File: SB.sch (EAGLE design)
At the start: 59 parts, among them IC1 ATMEGA32U4NT-TQFP, IC2 MCP2515, IC3 MCP2551, J1 USB-B-PTH, X1 INPUT, X2 OUTPUT

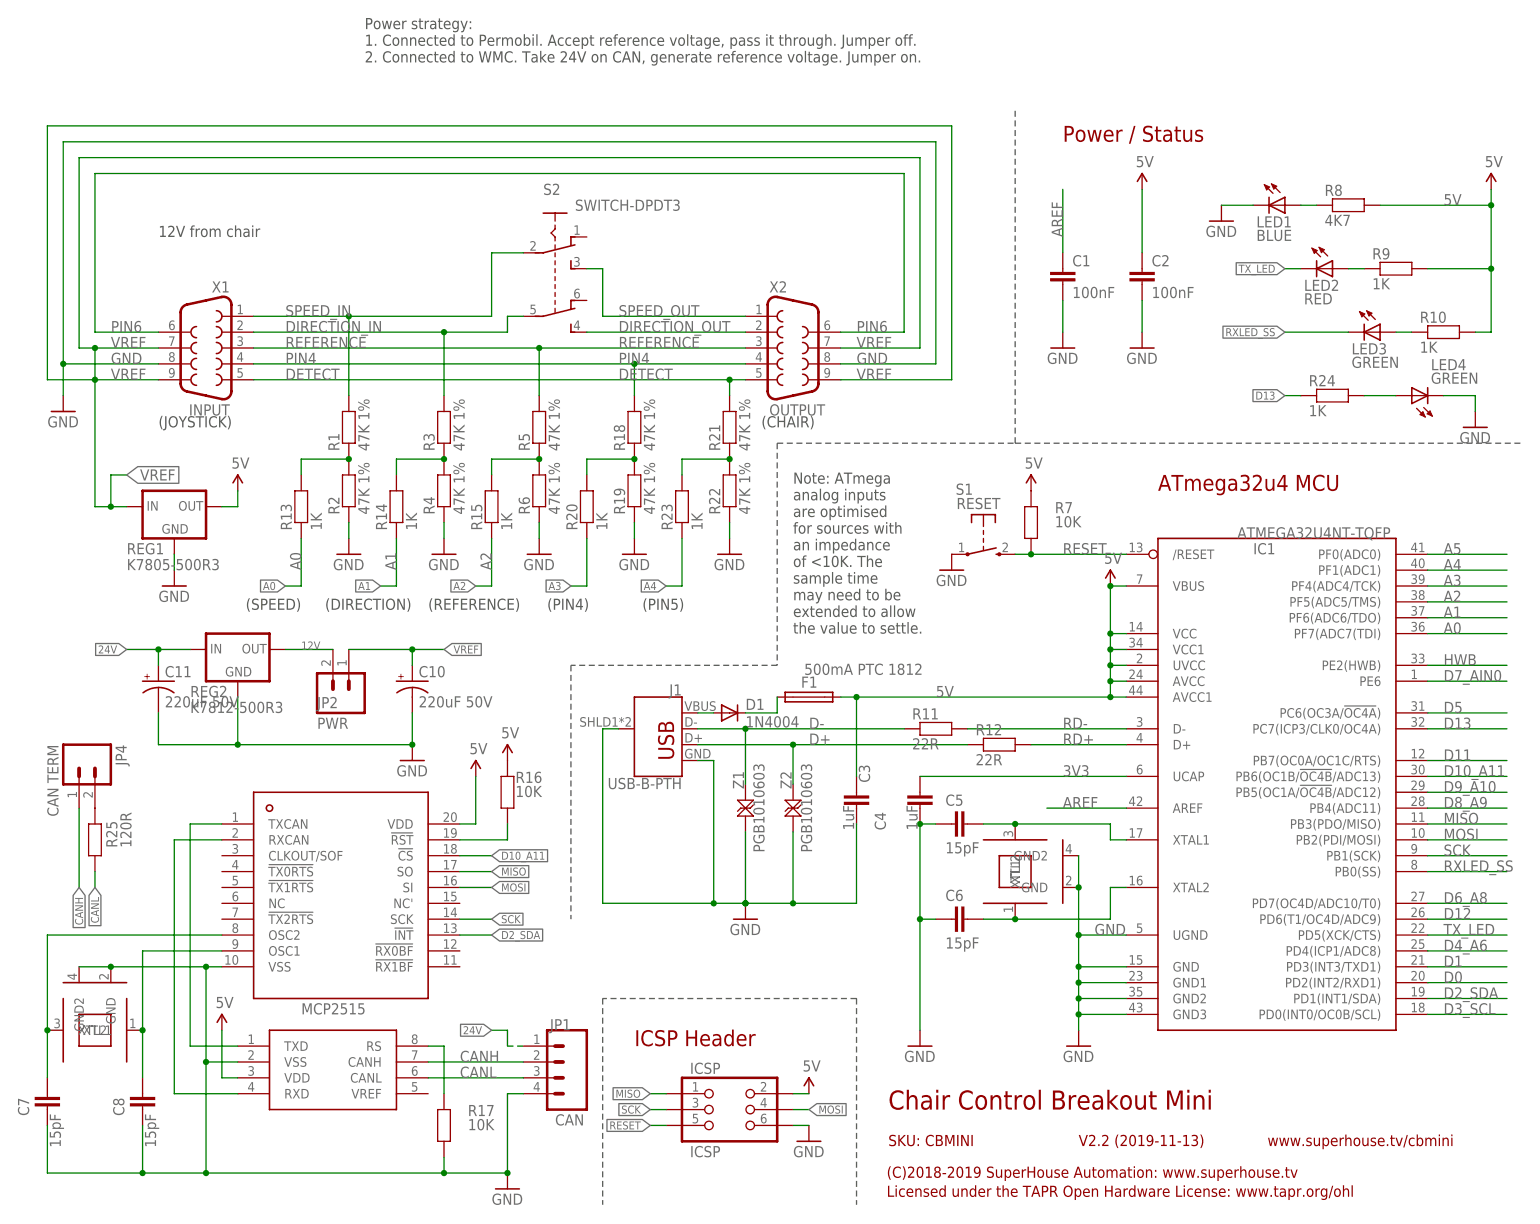
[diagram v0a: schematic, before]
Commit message: Basic schematic done and rough board outline
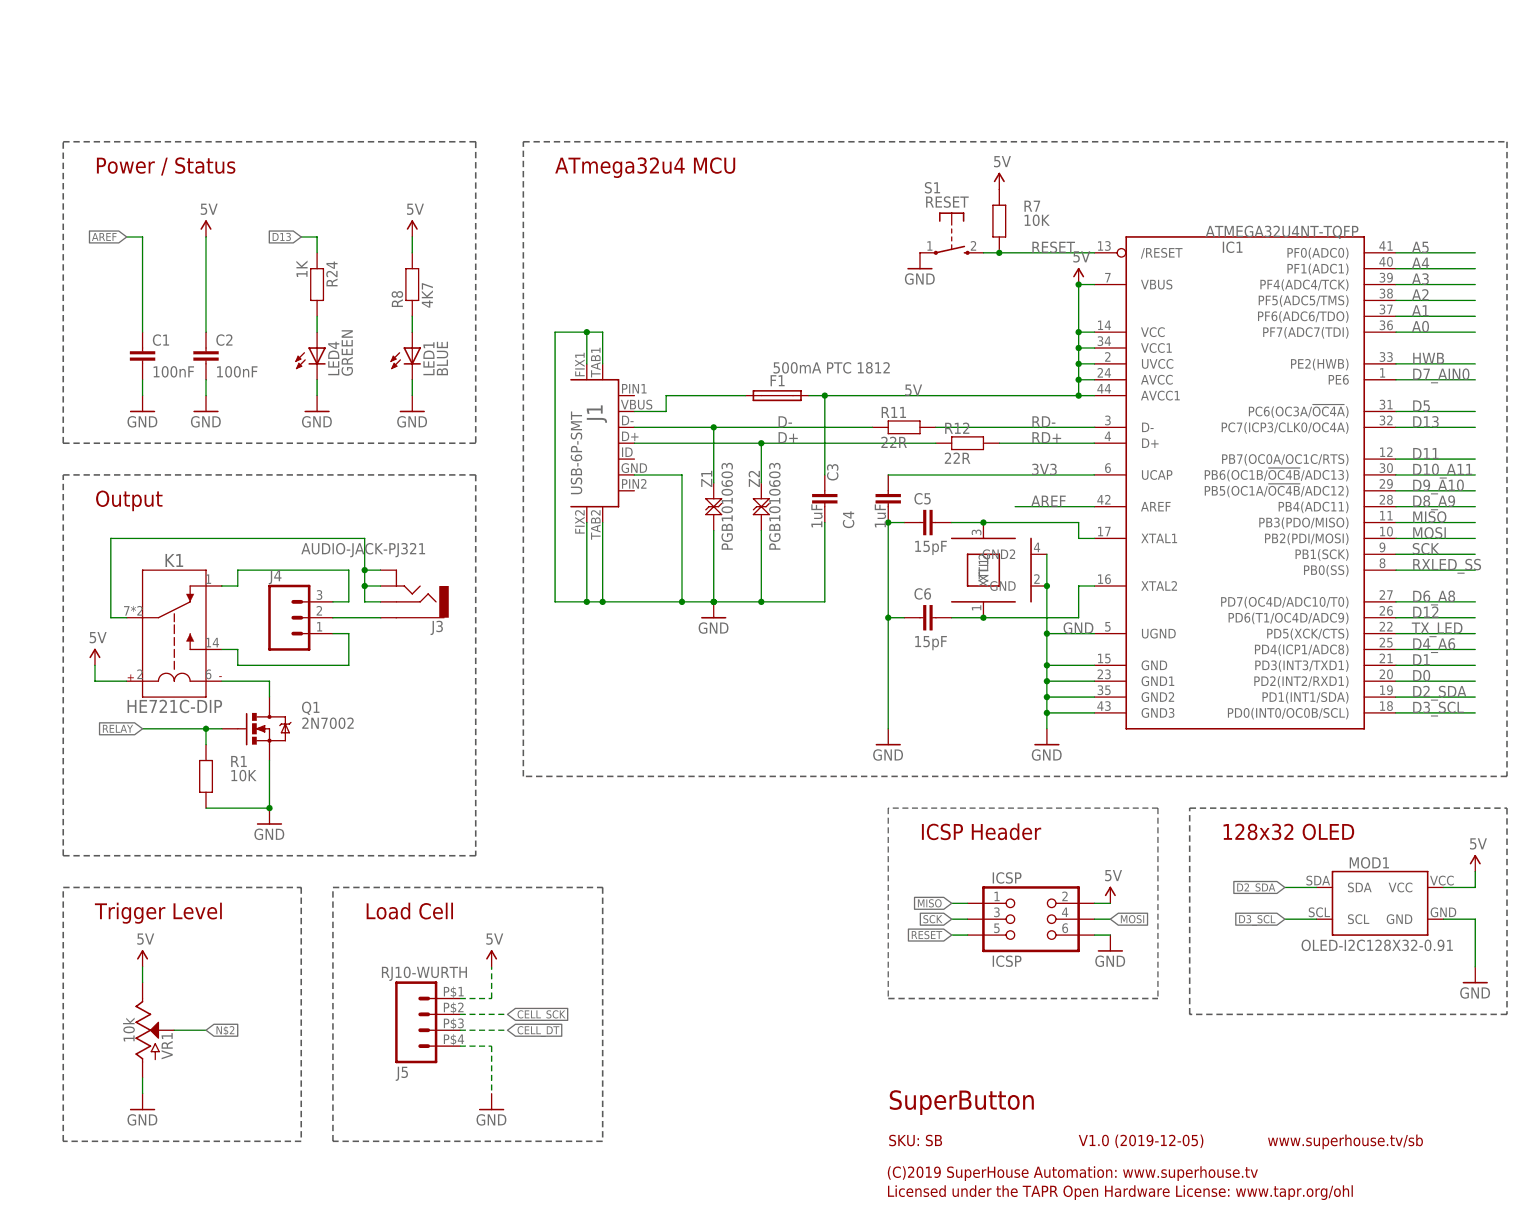
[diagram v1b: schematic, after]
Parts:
- removed C10, C11: 220uF 50V, SuperHouse-DiscreteSemi:CAP_POLG
- removed C7, C8: 15pF, SuperHouse-DiscreteSemi:CAP0603
- removed D1: 1N4004, SuperHouse-DiscreteSemi:DIODESMA
- removed IC2: MCP2515, SuperHouse-ICs:MCP2515
- removed IC3: MCP2551, SuperHouse-ICs:MCP2551
- removed JP1: CAN, SuperHouse-Connectors:M04-PIN
- removed JP2: PWR, SuperHouse-Connectors:M02-PIN
- removed JP4: CAN TERM, SuperHouse-Connectors:M02-PIN
- removed LED2: RED, SuperHouse-LEDs:LED0603
- removed LED3: GREEN, SuperHouse-LEDs:LED0603
- removed R10, R13, R14, R15, R20, R23, R9: 1K, SuperHouse-DiscreteSemi:RESISTOR0603
- removed R16, R17: 10K, SuperHouse-DiscreteSemi:RESISTOR0603
- removed R18, R19, R2, R21, R22, R3, R4, R5, R6: 47K 1%, SuperHouse-DiscreteSemi:RESISTOR0603
- removed R25: 120R, SuperHouse-DiscreteSemi:RESISTOR0603
- removed REG1: K7805-500R3, SuperHouse-Regulators:K78XX-500R3
- removed REG2: K7812-500R3, SuperHouse-Regulators:K78XX-500R3
- removed S2: SWITCH-DPDT3, freetronics-jon:SWITCH-DPDT3
- removed X1: INPUT, SparkFun-Connectors:DB9MALE
- removed X2: OUTPUT, SparkFun-Connectors:DB9FEMALE
- removed XTL2: 16MHz, SuperHouse-Oscillators:CRYSTAL-GND3X2
- added J3: AUDIO-JACK-PJ321, SuperHouse-Connectors:AUDIO-JACK-PJ321
- added J4: (no value), SuperHouse-Connectors:M03-PIN
- added J5: RJ10-WURTH, SuperHouse-Connectors:RJ10-WURTH
- added K1: HE721C-DIP, SuperHouse-Relays:HE721C-DIP
- added MOD1: OLED-I2C128X32-0.91, SuperHouse-Displays:OLED-I2C128X32-0.91
- added Q1: 2N7002, SuperHouse-DiscreteSemi:MOSFET-NCHANNEL-233
- added VR1: 10k, SuperHouse-DiscreteSemi:POTENTIOMETER-PTH-9MM-1/20W-20%-KIT
- J1: value USB-B-PTH -> USB-6P-SMT; device SuperHouse-Connectors:USB-B-PTH -> SuperHouse-Connectors:USB-6P-SMT
- R1: value 47K 1% -> 10K
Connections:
- removed net 12V: JP2.2, REG2.OUT
- removed net 24V: C11.+, JP1.1, REG2.IN
- removed net CANH: IC3.CANH, JP1.2, JP4.1
- removed net CANL: IC3.CANL, JP1.3, R25.1
- removed net DETECT: R21.2, X1.5, X2.5
- removed net DIRECTION_IN: R3.2, S2.5, X1.2
- removed net DIRECTION_OUT: S2.4, X2.2
- removed net N$10: IC2.!RST, R16.1
- removed net N$13: IC2.RXCAN, IC3.RXD
- removed net N$14: C8.2, IC2.OSC1, XTL2.XTL1
- removed net N$16: IC3.RS, R17.2
- removed net N$17: D1.C, F1.1
- removed net N$18: C7.2, IC2.OSC2, XTL2.XTL2
- removed net N$19: R18.1, R19.2, R20.2
- removed net N$20: JP4.2, R25.2
- removed net N$21: R21.1, R22.2, R23.2
- removed net N$8: LED3.A, R10.1
- removed net PIN4: R18.2, X1.4, X2.4
- removed net PIN6: X1.6, X2.6
- removed net REFERENCE: R5.2, X1.3, X2.3
- removed net SPEED_IN: R1.2, S2.2, X1.1
- removed net SPEED_OUT: S2.3, X2.1
- removed net VREF: C10.+, JP2.1, REG1.IN, X1.7, X1.9, X2.7, X2.9
- new net CELL_DT: J5.3
- new net CELL_SCK: J5.2
- new net N$6: J4.1, K1.NO
- new net RELAY: Q1.G, R1.2
- net 5V: now also J5.1, K1.COIL+, MOD1.VCC, VR1.E; no longer IC2.VDD, IC3.VDD, R10.2, R16.2, R9.2, REG1.OUT
- net A0: no longer R13.1
- net A1: no longer R14.1
- net A2: no longer R15.1
- net A3: no longer R20.1
- net A4: no longer R23.1
- net D10_A11: no longer IC2.!CS
- net D2_SDA: now also MOD1.SDA; no longer IC2.!INT
- net D3_SCL: now also MOD1.SCL
- net GND: now also J1.FIX1, J1.FIX2, J1.TAB1, J1.TAB2, J5.4, MOD1.GND, Q1.S, R1.1, VR1.A; no longer C10.-, C11.-, C7.1, C8.1, IC2.VSS, IC3.VSS, J1.SHIELD, JP1.4, R17.1, R19.1, R2.1, R22.1, R4.1, R6.1, REG1.GND, REG2.GND, X1.8, X2.8, XTL2.GND, XTL2.GND2
- net MISO: no longer IC2.SO
- net MOSI: no longer IC2.SI
- net N$2: now also VR1.S; no longer R1.1, R13.2, R2.2
- net N$3: now also K1.COIL-, Q1.D; no longer R14.2, R3.1, R4.2
- net N$4: now also J4.3, K1.NC; no longer R15.2, R5.1, R6.2
- net N$7: now also J3.2, J3.4A, J3.4B, K1.COM; no longer LED2.A, R9.1
- net N$9: now also J3.3, J4.2; no longer IC2.TXCAN, IC3.TXD
- net RXLED_SS: no longer LED3.C
- net SCK: no longer IC2.SCK
- net TX_LED: no longer LED2.C
- net USB+: now also F1.1; no longer D1.A
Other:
- note added: "(C)2019 SuperHouse Automation: www.superhouse.tv"
- note added: "128x32 OLED"
- note added: "Load Cell"
- note added: "Output"
- note added: "SKU: SB"
- note added: "SuperButton"
- note added: "Trigger Level"
- note added: "V1.0 (2019-12-05)"
- note added: "www.superhouse.tv/sb"
- note removed: "(C)2018-2019 SuperHouse Automation: www.superhouse.tv"
- note removed: "(CHAIR)"
- note removed: "(DIRECTION)"
- note removed: "(JOYSTICK)"
- note removed: "(PIN4)"
- note removed: "(PIN5)"
- note removed: "(REFERENCE)"
- note removed: "(SPEED)"
- note removed: "12V from chair"
- note removed: "Chair Control Breakout Mini"
- note removed: "Note: ATmega analog inputs are optimised for sources with an impedance of <10K. The sample time may need to be extended to allow the value to settle."
- note removed: "Power strategy: 1. Connected to Permobil. Accept reference voltage, pass it through. Jumper off. 2. Connected to WMC. Take 24V on CAN, generate reference voltage. Jumper on."
- note removed: "SKU: CBMINI"
- note removed: "V2.2 (2019-11-13)"
- note removed: "www.superhouse.tv/cbmini"
- moved on the sheet: C1, C2, C3, C4, C5, C6, F1, IC1, ICSP, LED1, LED4, R1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

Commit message: Replaced pot with rotary encoder, switched input and output sides
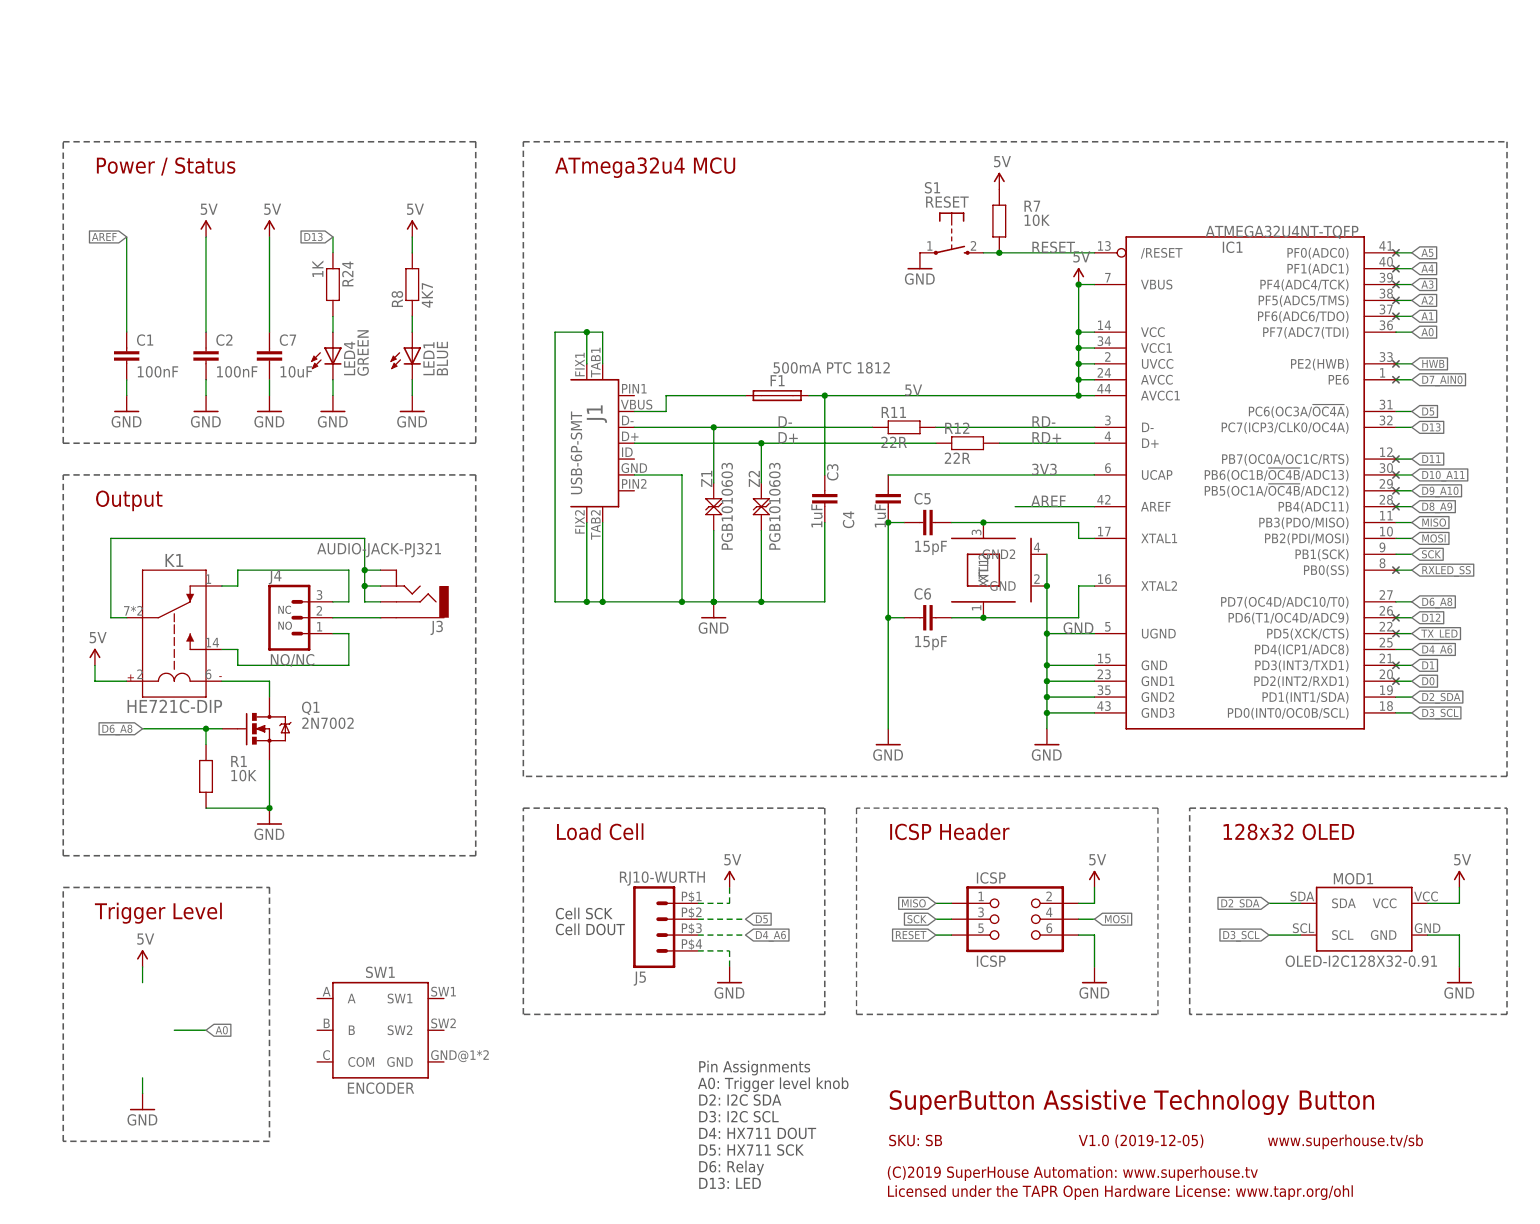
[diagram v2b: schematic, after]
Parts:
- removed VR1: 10k, SuperHouse-DiscreteSemi:POTENTIOMETER-PTH-9MM-1/20W-20%-KIT
- added C7: 10uF, SuperHouse-DiscreteSemi:CAP0805
- added SW1: ENCODER, SuperHouse-Switches:ENCODER
- J4: value (none) -> NO/NC
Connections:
- removed net CELL_DT: J5.3
- removed net CELL_SCK: J5.2
- removed net N$2: VR1.S
- removed net RELAY: Q1.G, R1.2
- net 5V: now also C7.1; no longer VR1.E
- net D4_A6: now also J5.3
- net D5: now also J5.2
- net D6_A8: now also Q1.G, R1.2
- net GND: now also C7.2; no longer VR1.A
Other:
- note added: "Cell DOUT"
- note added: "Cell SCK"
- note added: "NC"
- note added: "NO"
- note added: "Pin Assignments A0: Trigger level knob D2: I2C SDA D3: I2C SCL D4: HX711 DOUT D5: HX711 SCK D6: Relay D13: LED"
- note added: "SuperButton Assistive Technology Button"
- note removed: "SuperButton"
- moved on the sheet: C1, ICSP, J5, LED4, MOD1, R24

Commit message: Big cleanup of routing and silkscreen, with updated 3D model for OLED
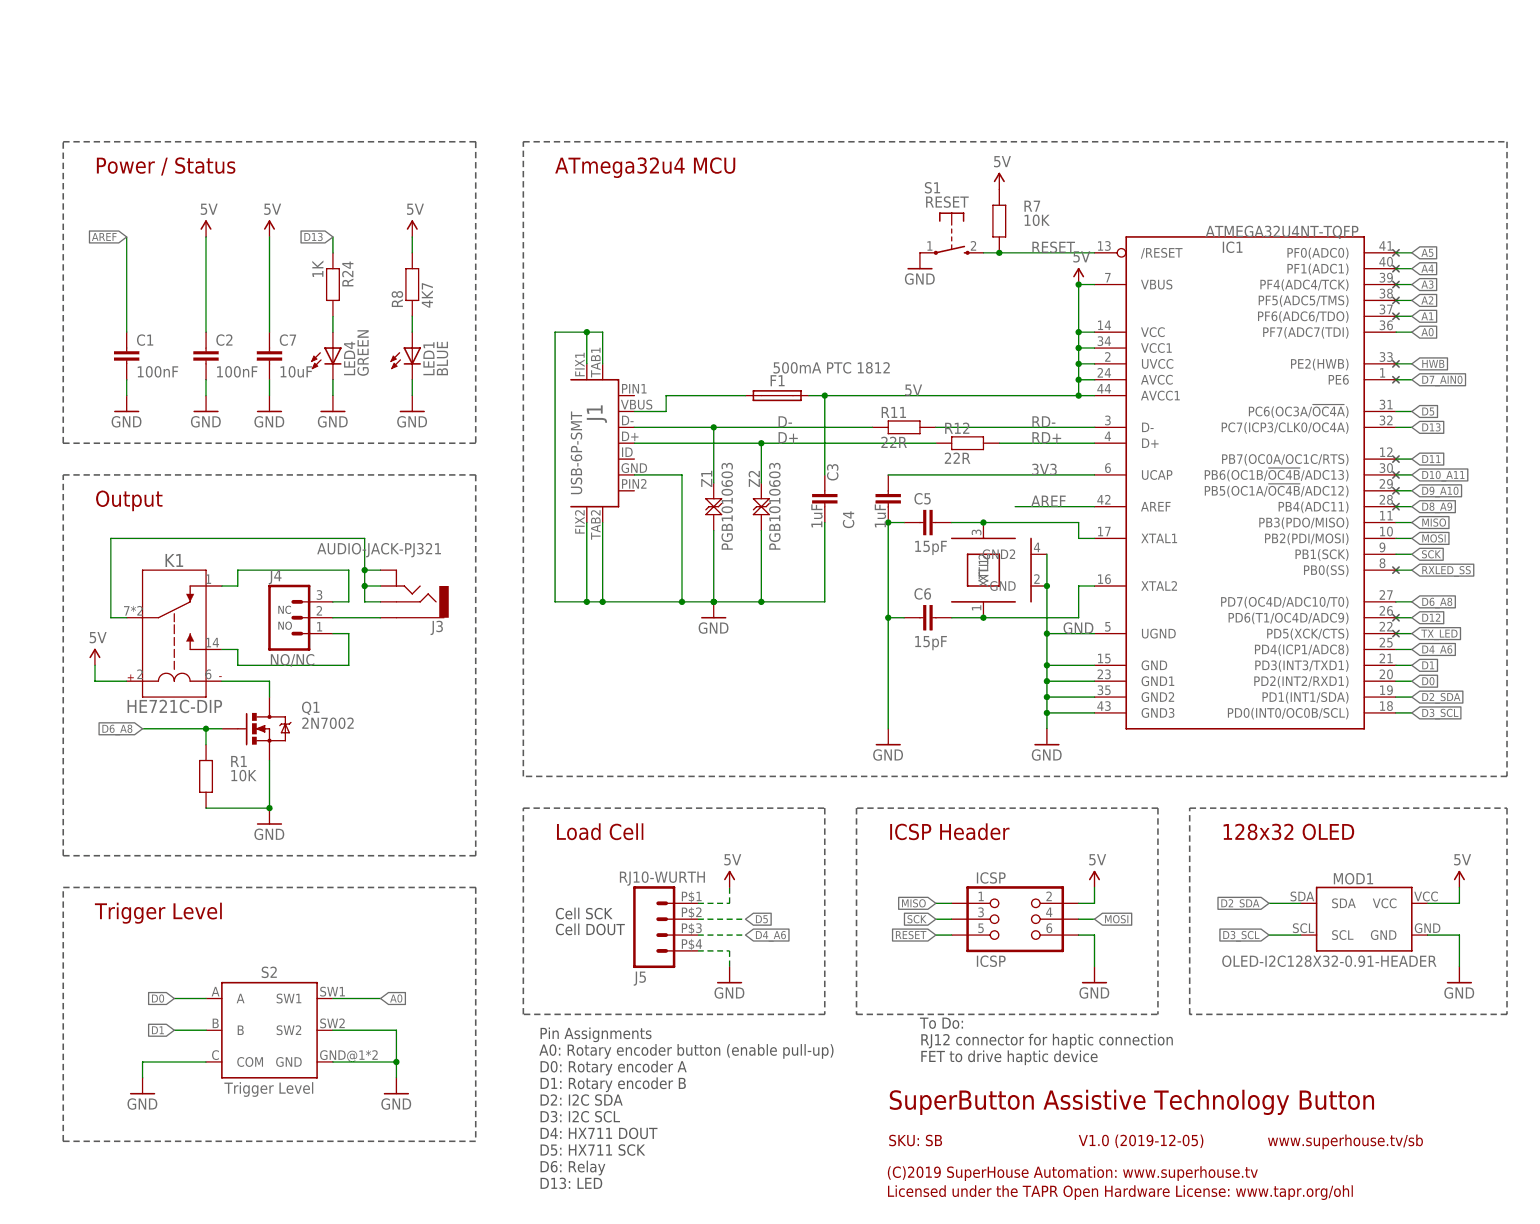
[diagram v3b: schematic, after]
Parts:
- removed SW1: ENCODER, SuperHouse-Switches:ENCODER
- added S2: Trigger Level, SuperHouse-Switches:ENCODER
- MOD1: value OLED-I2C128X32-0.91 -> OLED-I2C128X32-0.91-HEADER; device SuperHouse-Displays:OLED-I2C128X32-0.91 -> SuperHouse-Displays:OLED-I2C128X32-0.91-HEADER
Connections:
- net A0: now also S2.SW1
- net D0: now also S2.A
- net D1: now also S2.B
- net GND: now also S2.COM, S2.GND, S2.SW2
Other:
- note added: "Pin Assignments A0: Rotary encoder button (enable pull-up) D0: Rotary encoder A D1: Rotary encoder B D2: I2C SDA D3: I2C SCL D4: HX711 DOUT D5: HX711 SCK D6: Relay D13: LED"
- note added: "To Do: RJ12 connector for haptic connection FET to drive haptic device"
- note removed: "Pin Assignments A0: Trigger level knob D2: I2C SDA D3: I2C SCL D4: HX711 DOUT D5: HX711 SCK D6: Relay D13: LED"
